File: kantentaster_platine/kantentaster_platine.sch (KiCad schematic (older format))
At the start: 34 parts, among them IC1 PC817, P1 CONN_SENS, P2 CONN_12V, P3 CONN_OUTPUT, P4 lvl high test, P5 sens test, P6 lvl low test, P7 gnd test, Q1 BC817-40, U1 LM317_SOT223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

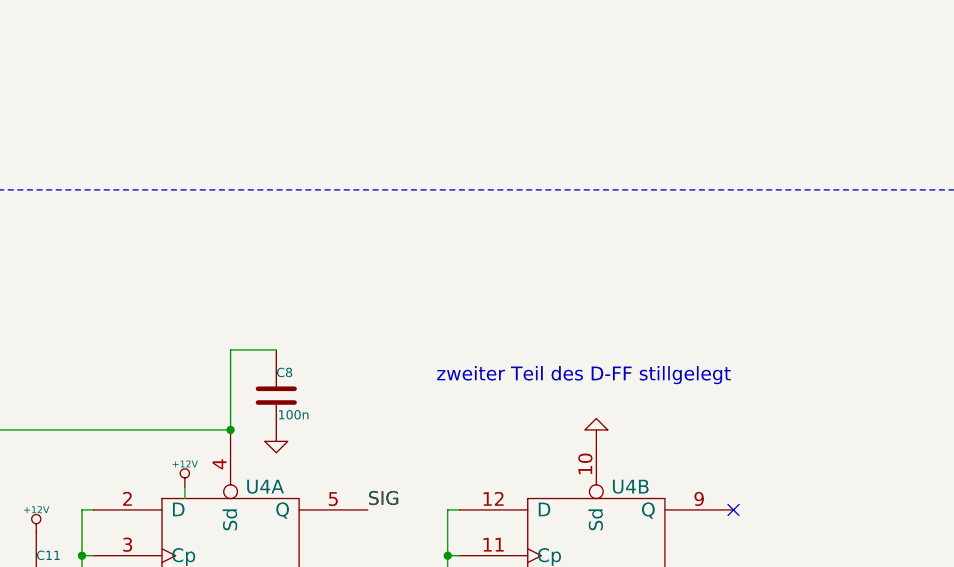
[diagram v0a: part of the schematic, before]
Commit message: Platine war Fail, TODO für nochmal machen ergänzt, wenn fertig mit neuen Bauteilen sauber aufbauen
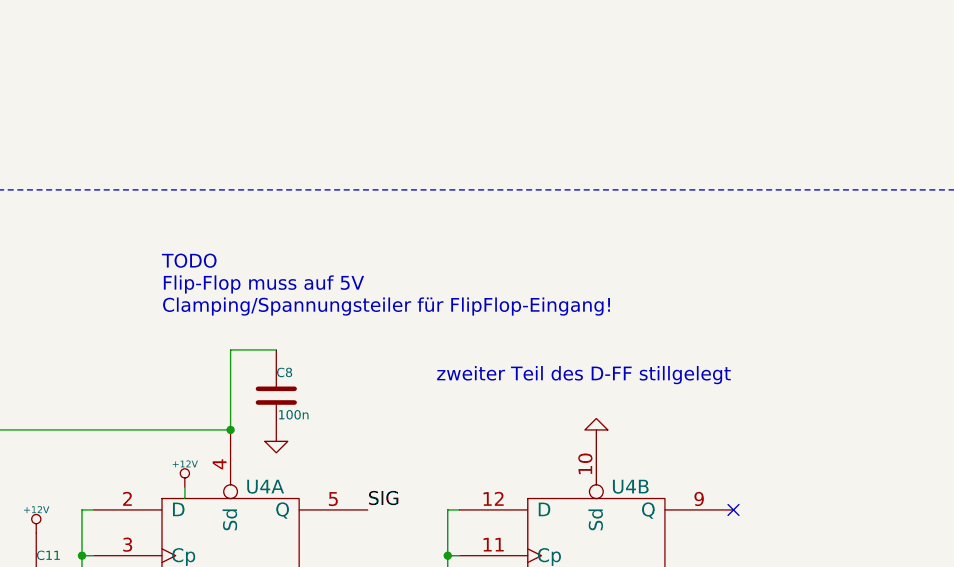
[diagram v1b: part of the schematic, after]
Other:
- note added: "TODO\nFlip-Flop muss auf 5V\nClamping/Spannungsteiler für FlipFlop-Eingang!\n"
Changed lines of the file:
@@
 	1    0    0    -1
 $EndComp
+Text Notes 7600 3300 0    60   ~ 0
+TODO\nFlip-Flop muss auf 5V\nClamping/Spannungsteiler für FlipFlop-Eingang!\n
 $EndSCHEMATC
